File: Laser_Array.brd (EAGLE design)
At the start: 160 x 100 mm, 131 parts, among them IC1 PIC24FJ64GA004, J3 22-23-2021, M1 MOTOR, U1 TCA9548A, U2 MAX6817, U3 LP2985-28DBVTE4, U4 TCA9548A, U5 LP2985A-33DBVTE4, X1 22-23-2031, X2 22-23-2041, X4 22-23-2041, X5 22-23-2041, X6 22-23-2031

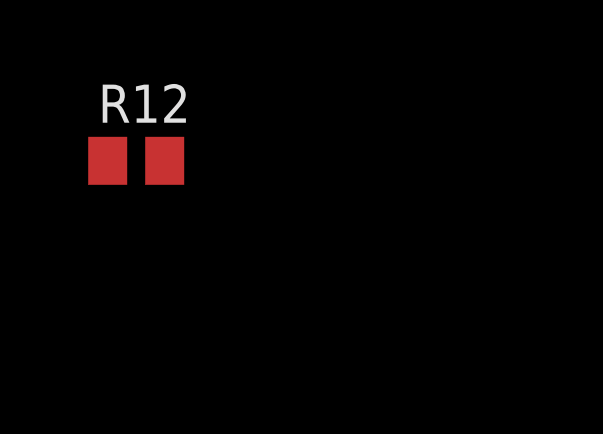
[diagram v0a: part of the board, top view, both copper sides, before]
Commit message: added MCU decoupling capacitor C17
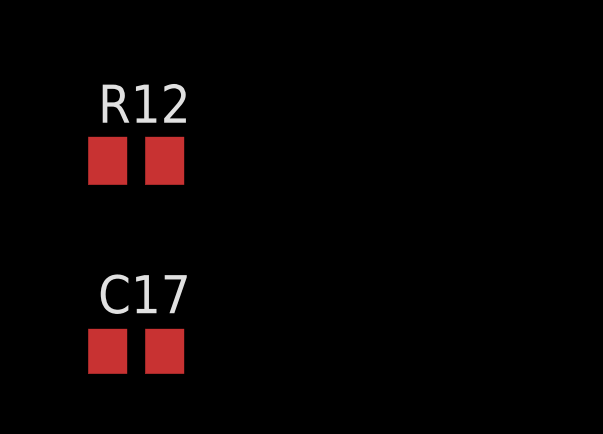
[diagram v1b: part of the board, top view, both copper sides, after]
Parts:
- added C17: 0.1uF, rcl:C0805
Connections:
- net GND: now also C17.2
- net VDD: now also C17.1
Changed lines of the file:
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@@
 <element name="R37" library="rcl" package="M0805" value="4.7k" x="22.86" y="273.05"/>
 <element name="R38" library="rcl" package="M0805" value="4.7k" x="27.94" y="273.05"/>
+<element name="C17" library="rcl" package="C0805" value="0.1uF" x="2.54" y="-1386.84"/>
 </elements>
 <signals>
@@
 <contactref element="R37" pad="1"/>
 <contactref element="R38" pad="1"/>
+<contactref element="C17" pad="1"/>
 <wire x1="2.775" y1="244.2178" x2="1.59" y2="250.19" width="0" layer="19" extent="1-1"/>
 <wire x1="1.59" y1="233.68" x2="2.775" y2="244.2178" width="0" layer="19" extent="1-1"/>
@@
 <wire x1="2.54" y1="-81.4" x2="3.49" y2="-76.2" width="0" layer="19" extent="1-1"/>
 <wire x1="3.49" y1="-88.9" x2="2.54" y2="-81.4" width="0" layer="19" extent="1-1"/>
-<wire x1="1.59" y1="-1380.49" x2="1.59" y2="250.19" width="0" layer="19" extent="1-1"/>
+<wire x1="1.59" y1="-1386.84" x2="1.59" y2="250.19" width="0" layer="19" extent="1-1"/>
+<wire x1="1.59" y1="-1380.49" x2="1.59" y2="-1386.84" width="0" layer="19" extent="1-1"/>
 <wire x1="1.59" y1="-1374.14" x2="1.59" y2="-1380.49" width="0" layer="19" extent="1-1"/>
 <wire x1="12.7" y1="-1362.71" x2="1.59" y2="-1374.14" width="0" layer="19" extent="1-1"/>
@@
 <contactref element="S18" pad="3"/>
 <contactref element="S19" pad="3"/>
+<contactref element="C17" pad="2"/>
 <wire x1="3.425" y1="238.3822" x2="4.725" y2="244.2178" width="0" layer="19" extent="1-1"/>
 <wire x1="9.925" y1="238.3822" x2="3.425" y2="238.3822" width="0" layer="19" extent="1-1"/>
@@
 <wire x1="9.925" y1="-1304.6678" x2="3.425" y2="-1304.6678" width="0" layer="19" extent="1-1"/>
 <wire x1="7.62" y1="-1362.71" x2="9.925" y2="-1304.6678" width="0" layer="19" extent="1-1"/>
+<wire x1="3.49" y1="-1386.84" x2="7.62" y2="-1362.71" width="0" layer="19" extent="1-1"/>
 </signal>
 <signal name="N$1">

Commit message: added CS and DC to schematic
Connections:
- net N$8 renamed DC
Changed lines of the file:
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@@
 <wire x1="103.886" y1="35.56" x2="70.17" y2="72.39" width="0" layer="19" extent="1-1"/>
 </signal>
-<signal name="N$8">
+<signal name="DC">
 <contactref element="J2" pad="3"/>
 <contactref element="IC1" pad="10"/>

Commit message: Started CPU Board
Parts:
- removed J2: (no value), Mine:22-23-2061
- added C19, C20: 10nF, rcl:C0805
- added SV1: (no value), con-lstb:MA12-2
- added SV2: (no value), con-lstb:MA17-2W
- moved C17 1344.3 mm to (-175.5, -54.3)
- moved R11 1344.3 mm to (-175.5, -41.6)
- moved R12 1344.3 mm to (-175.5, -48.0)
- moved R13 1344.3 mm to (-175.5, -12.4)
- moved R14 1344.3 mm to (-175.5, -18.8)
- moved R25 1344.3 mm to (-175.5, 6.62)
- moved U4 1344.3 mm to (-171.7, 30.8)
- moved X6 1344.3 mm to (-167.8, -30.2)
- moved LED26 1311.6 mm to (50.7, 121.0)
- moved R10 1311.6 mm to (43.0, 132.4)
- moved S25 1311.6 mm to (43.0, 140.1)
- moved S10 1073.3 mm to (-224.6, 60.2)
- moved S11 1073.3 mm to (-224.6, 39.9)
- moved S12 1073.3 mm to (-224.6, 19.6)
- moved S13 1073.3 mm to (-224.6, -0.75)
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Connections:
- removed net N$30: IC1.34
- removed net SCK1: X2.1, X5.1
- removed net SCLK1: IC1.44, R14.1, S3.4, U1.22, U4.22
- new net SCL1: IC1.44, R14.1, S3.4
- new net SCL2: IC1.24, U1.22, U4.22, X2.1, X5.1
- new net SDA2: IC1.23, U1.23, U4.23, X2.2, X5.2
- net A0: no longer IC1.33, U1.1, U4.1
- net CS: now also SV1.9; no longer J2.6
- net DC: now also SV1.11; no longer J2.3
- net ENCDR_A: now also IC1.36; no longer IC1.24
- net ENCDR_B: now also IC1.37; no longer IC1.23
- net GND: now also C19.2, C20.2, SV2.25, U4.1; no longer J2.2
- net MOSI: now also SV2.9; no longer J2.5
- net SCLK: now also SV2.11; no longer J2.4
- net SDA1: no longer U1.23, U4.23, X2.2, X5.2
- net VDD: now also C19.1, C20.1, SV2.29, U1.1; no longer J2.1

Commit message: temperture sensor board & CPU board complete
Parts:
- removed S28, S29, S30, S31, S32, S33, S34: TC74, Mine:SOT23-5L
- removed X6: 22-23-2031, Mine:22-23-2031
- added C21: 10nF, rcl:C0805
- added C22: 2.2uF, rcl:C0805
- added C23: 470uF, rcl:PANASONIC_F
- added D3, D4, D6: 641-1014-6-ND, adafruit:SOD-123
- added D5: S10M-TPMSCT_ND, Mine:S10M-TPMSCT-ND
- added D7, D8: LL4148FSCT-ND, semicon-smd-ipc:SOD80
- added J2, J4, J5, J7, J8, J9: 22-23-2021, Mine:22-23-2021
- added J6: (no value), Mine:RJ11-NO_SHIELD
- added R39: 4.7k, rcl:M0805
- added S20, S21, S22, S23, S24, S26, S27: TOGGLE_SPST, Mine:22-23-2021
- added X7, X8, X9: 22-23-2041, Mine:22-23-2041
- C1, C2: value 0.1uF -> 10F; device rcl:C0805 -> rcl:E5-10,5
- C10: value 10nF -> 10uF; device rcl:C0805 -> Mine:CAP3X3
- C11: value 10nF -> 18pF
- C12, C9: value 10nF -> 0.1uF
- C13: value 2.2uF -> 18pF
- C16: value 1uF -> 10nF
- C17: value 0.1uF -> 2.2uF
- C18: value 2.2uF -> 1uF
- C3: value 10uF -> 0.1uF
- C4: value 18pF -> 0.1uF
- C5: value 18pF -> 10uF
- C6: value 0.1uF -> 10nF
- C7: value 10uF -> 10nF; device Mine:CAP3X3 -> rcl:C0805
- D1: value LL4148FSCT-ND -> S10M-TPMSCT_ND; device semicon-smd-ipc:SOD80 -> Mine:S10M-TPMSCT-ND
- D2: value LL4148FSCT-ND -> 641-1014-6-ND; device semicon-smd-ipc:SOD80 -> adafruit:SOD-123
- J1: value (none) -> 22-23-2021; device Mine:RJ11-NO_SHIELD -> Mine:22-23-2021
- LED2: value LED3MM -> (none); device Mine:LED3MM -> Mine:LED5MM
- LED26: value (none) -> LED3MM; device Mine:LED5MM -> Mine:LED3MM
- Q1: device adafruit:SM49 -> Mine:SOT23-5L
- Q4: device Mine:SOT23-5L -> adafruit:SM49
- R1: value 10k -> 10R, 5W; device rcl:R0805 -> Mine:RESISTOR5W
- R10: value 330 -> 4.7k; device rcl:R0805 -> rcl:M0805
- R11: value 4.7k -> 330; device rcl:M0805 -> rcl:R0805
- R12: value 4.7k -> 220k
- R13: value 4.7k -> 200k; device rcl:M0805 -> rcl:RTRIM3224X
- R2: value 100k -> 10k
- R4: value 220k -> 100k; device rcl:M0805 -> rcl:R0805
- R5: value 200k -> 10k; device rcl:RTRIM3224X -> rcl:M0805
- R7: device rcl:M0805 -> rcl:R0805
- R8: value 10k -> 4.7k; device rcl:R0805 -> rcl:M0805
- S1: value TACT_PB -> (none); device Mine:PUSHBUTTON_SMD_SJ -> Mine:22-23-2061
- S10, S11, S12, S13, S14, S15, S4, S5, S6, S7, S8, S9: value TOGGLE_SPST -> TC74; device Mine:22-23-2021 -> Mine:SOT23-5L
- S16, S17, S18, S19, S25: value TC74 -> TOGGLE_SPST; device Mine:SOT23-5L -> Mine:22-23-2021
- S2: value (none) -> TACT_PB; device Mine:22-23-2061 -> Mine:PUSHBUTTON_SMD_SJ
- SV1: device con-lstb:MA12-2 -> con-lstb:MA17-2W
- SV2: device con-lstb:MA17-2W -> con-lstb:MA12-2
- U1: value TCA9548A -> MAX6817; device Mine:TSSOP24 -> Mine:SOT23-6
- U2: value MAX6817 -> LP2985-28DBVTE4; device Mine:SOT23-6 -> Texas Instruments_By_element14_Batch_1:SOT95P280X145-5N
- U3: value LP2985-28DBVTE4 -> TCA9548A; device Texas Instruments_By_element14_Batch_1:SOT95P280X145-5N -> Mine:TSSOP24
- X1: value 22-23-2031 -> 22-23-2041; device Mine:22-23-2031 -> Mine:22-23-2041
- moved C19 521.8 mm to (-236.0, -195.0)
- moved C2 474.5 mm to (-229.5, -282.0)
- moved D1 449.8 mm to (-250.5, -289.5)
- moved D2 446.3 mm to (-241.0, -296.5)
- moved X1 440.7 mm to (-243.0, -306.0)
- moved RLY2 436.7 mm to (-237.5, -418.5)
- moved J3 420.9 mm to (-243.0, -381.5)
- moved R1 420.1 mm to (-239.0, -230.0)
- moved S16 401.2 mm to (270.9, -2.37)
- moved C18 370.4 mm to (-230.0, -195.0)
- moved C1 345.6 mm to (-229.5, -79.0)
- moved S25 323.3 mm to (-224.6, -41.4)
- moved C8 298.2 mm to (-175.5, -54.3)
- moved R11 279.4 mm to (43.0, 132.4)
- moved X2 272.9 mm to (-233.5, -247.5)
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- renumbered X4 to X3
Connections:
- removed net A0: X2.3, X5.3
- removed net ENSW: U2.1, X3.4
- removed net N$14: U2.6
- new net CHGOUTA: IC1.2, J9.1
- new net CHGOUTB: IC1.3, J9.2
- new net ENSW_I: U1.1, X3.4
- new net ENSW_O: IC1.15, U1.6
- new net N$30: J1.1, LED1.A
- new net N$31: C19.1, U5.4
- new net N$32: J2.2, Q1.5
- new net N$33: D3.C, D4.A, R1.2
- new net N$34: J7.1, Q3.5
- new net N$36: C1.-, C2.+
- new net N$37: C1.+, D5.A, R1.1
- new net N$8: D1.A, D2.C
- new net VLASER: D1.C, RLY1.3, X1.4, X2.4, X8.4, X9.4
- net !RESET: now also R14.2, R15.2, U3.3, X8.3, X9.3; no longer R25.2, R30.2, U1.3, X2.4, X5.4
- net +12V: now also C18.1, J2.1, R12.2, U2.1, U2.3, X2.2, X5.3, X7.3; no longer C16.1, LED1.A, R4.2, U3.1, U3.3, X1.2, X6.2
- net +12V_TB: now also D6.C, RLY2.1, X1.2
- net CHGA: now also J8.1; no longer J3.1
- net CHGB: now also J8.2; no longer J3.2
- net CS: now also SV2.9; no longer SV1.9
- net DC: now also SV2.11; no longer SV1.11
- net ENCDR_A: now also C7.1, R5.1; no longer C11.1, R7.1
- net ENCDR_B: now also C6.1; no longer C10.1
- net EXFAN: now also Q2.1, R4.1; no longer Q3.1, R3.1
- net GND: now also C10.-, C2.-, C21.2, C22.2, C23.-, C7.2, C9.1, D8.2, J3.2, J4.2, J5.2, J6.4, J7.2, LED26.K, LED8.K, Q1.2, R11.1, R13.1, R4.2, RLY2.2, S1.4, S10.2, S11.2, S12.2, S13.2, S14.2, S15.2, S2.1, S2.2, S4.2, S5.2, S6.2, S7.2, S8.2, S9.2, SV1.25, U3.1, U3.12, U3.21, X1.3, X2.3, X5.4, X7.4; no longer C1.1, C10.2, C2.2, C7.-, C9.2, D2.2, J1.4, LED14.K, LED2.K, Q4.2, R10.1, R2.2, R5.1, S1.1, S1.2, S16.3, S17.3, S18.3, S19.3, S2.4, S25.3, S28.3, S29.3, S30.3, S31.3, S32.3, S33.3, S34.3, SV2.25, U1.12, U1.21, U4.1, X1.1, X6.1
- net LASOUT: now also LED2.A, RLY2.5; no longer LED26.A, RLY2.2
- net LASRLY: now also Q3.1; no longer Q4.1
- net MOSI: now also SV1.9; no longer SV2.9
- net N$1: now also C10.+, J6.6, R7.2, S2.3, S2.4; no longer C7.+, J1.6, R1.2, S1.3, S1.4
- net N$10: now also U1.4; no longer U2.4
- net N$11: now also J1.2; no longer Q2.5
- net N$12: now also J3.1, Q2.5; no longer M1.1, Q3.5
- net N$13: now also R13.3; no longer R5.3
- net N$15: now also D6.A, J5.1; no longer Q4.5
- net N$16: now also LED17.A, S18.1; no longer LED18.A, S6.1
- net N$17: now also RLY2.4, S16.2, S17.2, S18.2, S19.2, S20.2, S21.2, S22.2, S23.2, S24.2, S25.2, S26.2, S27.2; no longer RLY2.3, S10.2, S11.2, S12.2, S13.2, S14.2, S15.2, S4.2, S5.2, S6.2, S7.2, S8.2, S9.2
- net N$18: now also LED15.A, LED3.A, S16.1; no longer LED16.A, LED2.A, S4.1
- net N$19: now also LED16.A, LED9.A, S17.1; no longer LED15.A, LED3.A, S5.1
- net N$2: now also C5.1; no longer C3.1
- net N$20: now also LED10.A, LED18.A, S19.1; no longer LED21.A, LED5.A, S7.1
- net N$21: now also LED19.A, LED5.A, S20.1; no longer LED17.A, LED6.A, S9.1
- net N$22: now also LED11.A, LED20.A, S21.1; no longer LED25.A, LED7.A, S10.1
- net N$23: now also LED21.A, LED6.A, S22.1; no longer LED13.A, LED23.A, S11.1
- net N$24: now also LED22.A, S23.1; no longer LED19.A, S12.1
- net N$25: now also LED23.A, LED7.A, S24.1; no longer LED11.A, LED14.A, S14.1
- net N$26: now also LED13.A, LED24.A, S25.1; no longer LED10.A, LED20.A, S15.1
- net N$27: now also LED25.A, LED8.A, S26.1; no longer LED22.A, LED9.A, S8.1
- net N$28: now also LED14.A, LED26.A, S27.1; no longer LED24.A, LED8.A, S13.1
- net N$29: now also LED2.K, R11.2; no longer LED26.K, R10.2
- net N$3: now also J6.1; no longer J1.1
- net N$35: now also J4.1, M1.1; no longer C12.1, U5.4
- net N$4: now also J6.2; no longer J1.2
- net N$5: now also J6.3; no longer J1.3
- net N$55: now also U2.4; no longer U3.4
- net N$6: now also C11.1, Q4.1; no longer C5.1, Q1.1
- net N$7: now also C13.1, Q4.2; no longer C4.1, Q1.2
- net N$9: now also R2.1, S1.2, U1.3; no longer R8.1, S2.2, U2.3
- net ONLED: now also Q1.1, R3.1; no longer Q2.1, R2.1
- net SC0: now also R22.2, S4.4, U3.5; no longer R12.2, S25.4, U4.5
- net SC1: now also R34.2, S10.4, U3.7; no longer R16.2, S28.4, U4.7
- net SC10: now also R27.2, S9.4, U4.9; no longer R36.2, S18.4, U1.9
- net SC11: now also R39.2, S15.4, U4.11; no longer R38.2, S19.4, U1.11
- net SC2: now also R23.2, S5.4, U3.9; no longer R18.2, S29.4, U4.9
- net SC3: now also R35.2, S11.4, U3.11; no longer R20.2, S30.4, U4.11
- net SC4: now also R24.2, S6.4, U3.14; no longer R22.2, S31.4, U4.14
- net SC5: now also R36.2, S12.4, U3.16; no longer R24.2, S32.4, U4.16
- net SC6: now also R25.2, S7.4, U3.18; no longer R27.2, S33.4, U4.18
- net SC7: now also R37.2, S13.4, U3.20; no longer R29.2, S34.4, U4.20
- net SC8: now also R26.2, S8.4, U4.5; no longer R32.2, S16.4, U1.5
- net SC9: now also R38.2, S14.4, U4.7; no longer R34.2, S17.4, U1.7
- net SCL1: now also R10.1; no longer R14.1
- net SCL2: now also U3.22, X8.1, X9.1; no longer U1.22, X2.1, X5.1
- net SCLK: now also SV1.11; no longer SV2.11
- net SD0: now also R16.2, S4.5, U3.4; no longer R11.2, S25.5, U4.4
- net SD1: now also R28.2, S10.5, U3.6; no longer R15.2, S28.5, U4.6
- net SD10: now also R21.2, S9.5, U4.8; no longer R35.2, S18.5, U1.8
- net SD11: now also R33.2, S15.5, U4.10; no longer R37.2, S19.5, U1.10
- net SD2: now also S5.5, U3.8; no longer S29.5, U4.8
- net SD3: now also R29.2, S11.5, U3.10; no longer R19.2, S30.5, U4.10
- net SD4: now also R18.2, S6.5, U3.13; no longer R21.2, S31.5, U4.13
- net SD5: now also R30.2, S12.5, U3.15; no longer R23.2, S32.5, U4.15
- net SD6: now also R19.2, S7.5, U3.17; no longer R26.2, S33.5, U4.17
- net SD7: now also R31.2, S13.5, U3.19; no longer R28.2, S34.5, U4.19
- net SD8: now also R20.2, S8.5, U4.4; no longer R31.2, S16.5, U1.4
- net SD9: now also R32.2, S14.5, U4.6; no longer R33.2, S17.5, U1.6
- net SDA1: now also R8.1; no longer R13.1
- net SDA2: now also U3.23, X8.2, X9.2; no longer U1.23, X2.2, X5.2
- net VDD: now also C12.1, C21.1, C3.1, C4.1, C9.2, D4.C, D5.C, J6.5, R10.2, R14.1, R2.2, R39.1, R5.2, R7.1, SV1.29, U1.5, U3.24, U4.1, X5.1, X7.1; no longer C1.2, C17.1, C19.1, C2.1, C6.1, J1.5, R1.1, R11.1, R12.1, R13.2, R14.2, R7.2, S3.3, SV2.29, U1.1, U1.24, U2.5, X1.3, X6.3
- net VDD_TB: now also D2.A, D3.A, X1.1, X2.1; no longer RLY1.3
- net VIN1: now also C16.1, D7.2, D8.1, R12.1, R13.2; no longer C9.1, D1.2, D2.1, R4.1, R5.2
- net VRR: now also C17.1, D7.1, U2.5; no longer C18.1, D1.1, U3.5
- net VTS: now also C22.1, C23.+, S10.3, S11.3, S12.3, S13.3, S14.3, S15.3, S3.3, S4.3, S5.3, S6.3, S7.3, S8.3, S9.3, X5.2, X7.2; no longer C13.1, S16.2, S17.2, S18.2, S19.2, S25.2, S28.2, S29.2, S30.2, S31.2, S32.2, S33.2, S34.2
